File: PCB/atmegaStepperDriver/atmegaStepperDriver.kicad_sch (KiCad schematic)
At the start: 74 parts, among them J1 General power, J2 Motor Output, J3 Motor power, J4 Conn_01x05_Socket, J5 Reset Header, J6 I2C Communication pins, J9 Stepper communication pins, Q1 TIP42C, Q10 BC547, Q11 BC557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

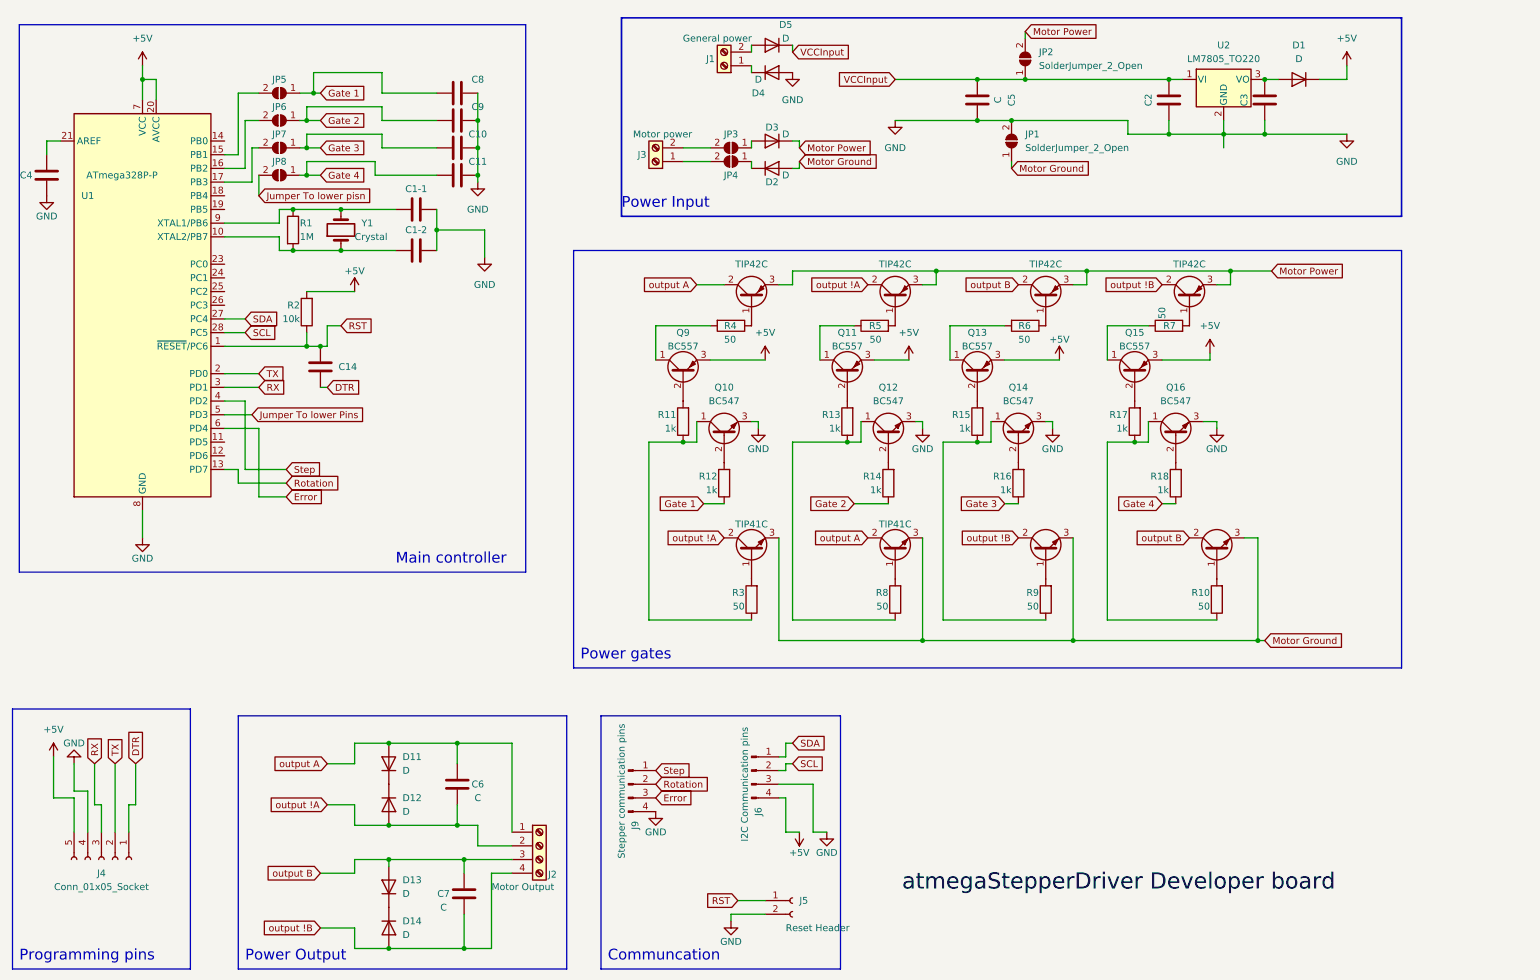
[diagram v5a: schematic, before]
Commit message: change capacitor footprint; added few pictures;
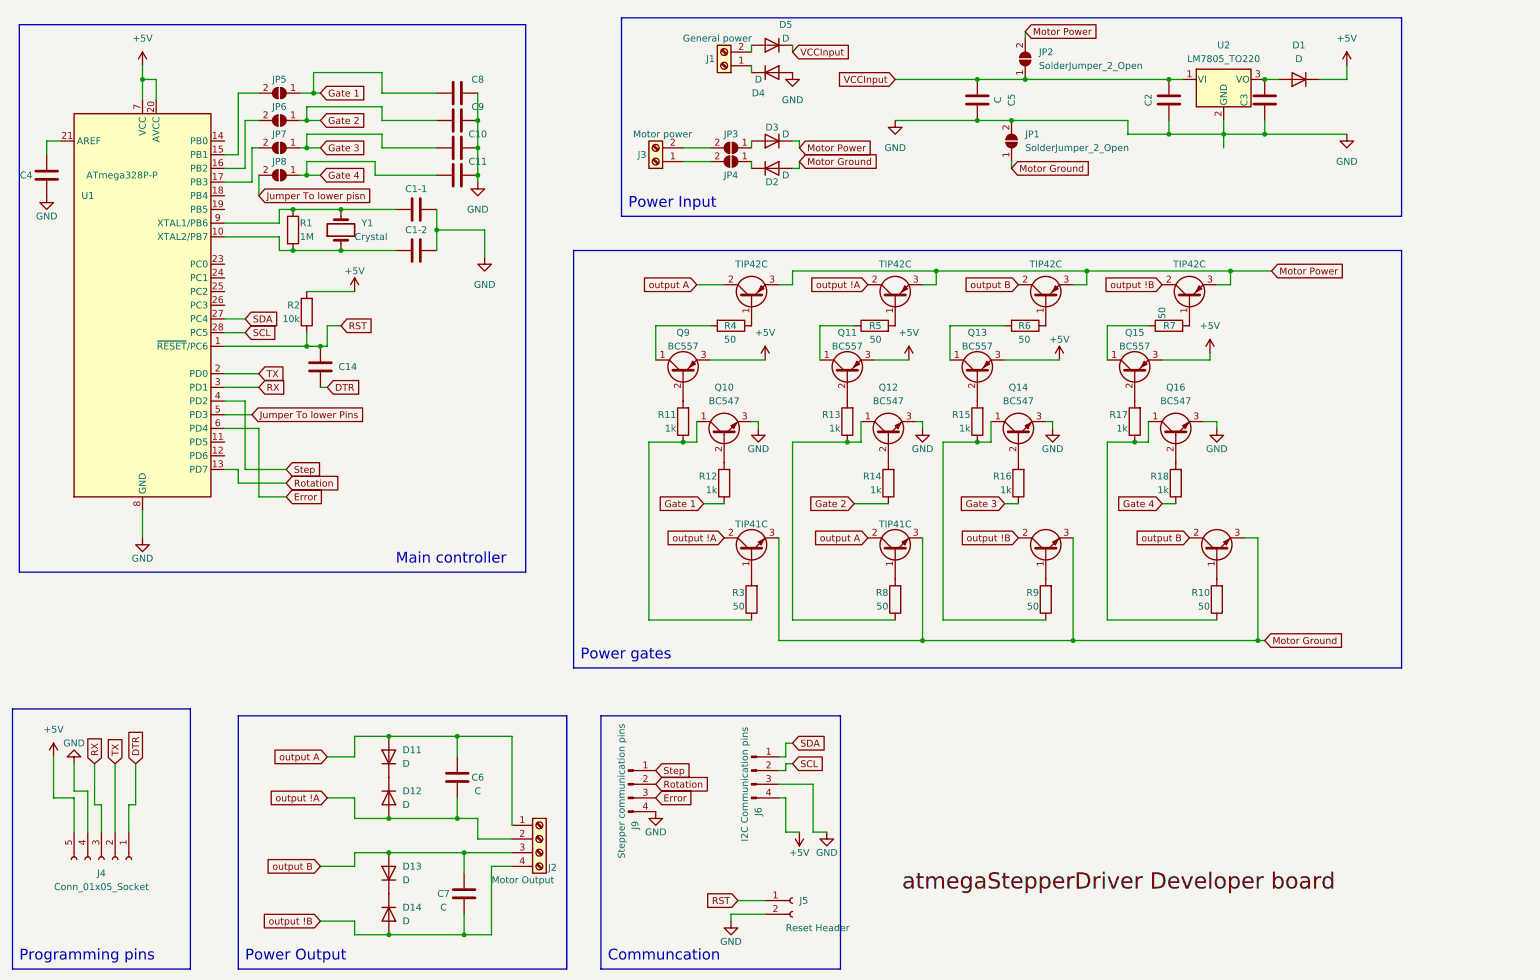
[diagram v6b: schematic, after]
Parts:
- C5: footprint Capacitor_THT:CP_Radial_Tantal_D9.0mm_P5.00mm -> Capacitor_THT:CP_Radial_D10.0mm_P5.00mm
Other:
- moved on the sheet: C6, D11, D12, D13, D14, J2

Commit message: All general connections ready; further check needed; V0.0.6
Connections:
- net Jumper To lower pisn is gone; now on net Jumper To lower Pins: JP8.2 (B)
- net GND: now also D2.2 (A), Q2.3 (E), Q6.3 (E), Q7.3 (E), Q8.3 (E)
- net Motor Ground: no longer D2.2 (A), Q2.3 (E), Q6.3 (E), Q7.3 (E), Q8.3 (E)
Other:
- moved on the sheet: C1-1, C1-2, C10, C11, C14, C2, C3, C4, C5, C6, C7, C8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

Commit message: Footprint done; ready for testing; drc clear; Gerber files;V0.7.1;
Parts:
- removed JP1: SolderJumper_2_Open, Jumper:SolderJumper-2_P1.3mm_Open_RoundedPad1.0x1.5mm, symbol Jumper:SolderJumper_2_Open
- added D6: D, Diode_THT:D_A-405_P7.62mm_Horizontal, symbol Device:D
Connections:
- net Motor Power: now also JP2.1 (A); no longer JP2.2 (B)
- net VCCInput: now also D6.2 (A); no longer JP2.1 (A)
- new net: D6.1 (K), JP2.2 (B)
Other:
- title: (none) -> atmegaStepperDriver Developer board
- moved on the sheet: JP2
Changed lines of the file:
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@@
   (paper "A4")
   (title_block
-    (date "2023-08-07")
-    (rev "0.0.6")
+    (title "atmegaStepperDriver Developer board")
+    (date "2023-08-09")
+    (rev "v0.7.1")
   )
   (junction (at 69.85 53.34) (diameter 0) (color 0 0 0 0)
@@
   (junction (at 76.2 59.69) (diameter 0) (color 0 0 0 0)
   )
-  (junction (at 195.58 29.21) (diameter 0) (color 0 0 0 0)
-  )
   (junction (at 71.12 38.1) (diameter 0) (color 0 0 0 0)
   )
@@
   (junction (at 81.28 165.1) (diameter 0) (color 0 0 0 0)
   )
+  (junction (at 194.31 29.21) (diameter 0) (color 0 0 0 0)
+  )
   (junction (at 195.58 92.71) (diameter 0) (color 0 0 0 0)
   )
@@
   (junction (at 81.28 143.51) (diameter 0) (color 0 0 0 0)
   )
-  (junction (at 193.04 36.83) (diameter 0) (color 0 0 0 0)
-  )
   (junction (at 81.28 180.34) (diameter 0) (color 0 0 0 0)
   )
@@
     (stroke (width 0) (type default))
   )
-  (wire (pts (xy 195.58 20.32) (xy 195.58 21.59))
+  (wire (pts (xy 195.58 20.32) (xy 194.31 20.32))
     (stroke (width 0) (type default))
   )
@@
     (stroke (width 0) (type default))
   )
+  (wire (pts (xy 179.07 20.32) (xy 179.07 26.67))
+    (stroke (width 0) (type default))
+  )
   (wire (pts (xy 57.15 110.49) (xy 66.04 110.49))
     (stroke (width 0) (type default))
@@
     (stroke (width 0) (type default))
   )
-  (wire (pts (xy 186.69 36.83) (xy 193.04 36.83))
+  (wire (pts (xy 186.69 36.83) (xy 214.63 36.83))
     (stroke (width 0) (type default))
   )
@@
     (stroke (width 0) (type default))
   )
-  (wire (pts (xy 195.58 29.21) (xy 222.25 29.21))
-    (stroke (width 0) (type default))
-  )
   (wire (pts (xy 58.42 43.18) (xy 58.42 52.07))
     (stroke (width 0) (type default))
@@
     (stroke (width 0) (type default))
   )
+  (wire (pts (xy 194.31 29.21) (xy 222.25 29.21))
+    (stroke (width 0) (type default))
+  )
   (wire (pts (xy 160.02 152.4) (xy 153.67 152.4))
     (stroke (width 0) (type default))
@@
     (stroke (width 0) (type default))
   )
-  (wire (pts (xy 193.04 36.83) (xy 214.63 36.83))
-    (stroke (width 0) (type default))
-  )
   (wire (pts (xy 198.12 88.9) (xy 198.12 92.71))
     (stroke (width 0) (type default))
@@
     (stroke (width 0) (type default))
   )
+  (wire (pts (xy 179.07 26.67) (xy 194.31 26.67))
+    (stroke (width 0) (type default))
+  )
   (wire (pts (xy 69.85 82.55) (xy 69.85 85.09))
     (stroke (width 0) (type default))
@@
     (stroke (width 0) (type default))
   )
+  (wire (pts (xy 194.31 26.67) (xy 194.31 29.21))
+    (stroke (width 0) (type default))
+  )
   (wire (pts (xy 69.85 50.8) (xy 69.85 53.34))
     (stroke (width 0) (type default))
@@
     (stroke (width 0) (type default))
   )
-  (wire (pts (xy 186.69 29.21) (xy 195.58 29.21))
+  (wire (pts (xy 186.69 29.21) (xy 194.31 29.21))
     (stroke (width 0) (type default))
   )
@@
     )
   )
-  (global_label "Motor Ground" (shape input) (at 193.04 45.72 0) (fields_autoplaced)
-    (effects (font (size 1.27 1.27)) (justify left))
-    (property "Intersheetrefs" "${INTERSHEET_REFS}" (at 208.9063 45.72 0)
-      (effects (font (size 1.27 1.27)) (justify left) hide)
-    )
-  )
   (global_label "output !B" (shape input) (at 203.2 110.49 180) (fields_autoplaced)
     (effects (font (size 1.27 1.27)) (justify right))
@@
     )
   )
-  (symbol (lib_id "Jumper:SolderJumper_2_Open") (at 193.04 40.64 90) (unit 1)
-    (in_bom yes) (on_board yes) (dnp no) (fields_autoplaced)
-    (property "Reference" "JP1" (at 195.58 39.37 90)
-      (effects (font (size 1.27 1.27)) (justify right))
-    )
-    (property "Value" "SolderJumper_2_Open" (at 195.58 41.91 90)
-      (effects (font (size 1.27 1.27)) (justify right))
-    )
-    (property "Footprint" "Jumper:SolderJumper-2_P1.3mm_Open_RoundedPad1.0x1.5mm" (at 193.04 40.64 0)
-      (effects (font (size 1.27 1.27)) hide)
-    )
-    (property "Datasheet" "~" (at 193.04 40.64 0)
-      (effects (font (size 1.27 1.27)) hide)
-    )
-    (pin "1")
-    (pin "2")
-    (instances
-      (project "atmegaStepperDriver"
-        (path "/c84e7e69-c1fd-4499-93bc-6ad0c4ebade1"
-          (reference "JP1") (unit 1)
-        )
-      )
-    )
-  )
   (symbol (lib_id "Transistor_BJT:BC557") (at 195.58 80.01 90) (unit 1)
     (in_bom yes) (on_board yes) (dnp no)
@@
     )
   )
-  (symbol (lib_id "Jumper:SolderJumper_2_Open") (at 195.58 25.4 90) (unit 1)
-    (in_bom yes) (on_board yes) (dnp no) (fields_autoplaced)
-    (property "Reference" "JP2" (at 198.12 24.13 90)
-      (effects (font (size 1.27 1.27)) (justify right))
-    )
-    (property "Value" "SolderJumper_2_Open" (at 198.12 26.67 90)
-      (effects (font (size 1.27 1.27)) (justify right))
-    )
-    (property "Footprint" "Jumper:SolderJumper-2_P1.3mm_Open_RoundedPad1.0x1.5mm" (at 195.58 25.4 0)
-      (effects (font (size 1.27 1.27)) hide)
-    )
-    (property "Datasheet" "~" (at 195.58 25.4 0)
+  (symbol (lib_id "Jumper:SolderJumper_2_Open") (at 190.5 20.32 180) (unit 1)
+    (in_bom yes) (on_board yes) (dnp no)
+    (property "Reference" "JP2" (at 193.04 25.4 0)
+      (effects (font (size 1.27 1.27)))
+    )
+    (property "Value" "SolderJumper_2_Open" (at 195.58 22.86 0)
+      (effects (font (size 1.27 1.27)))
+    )
+    (property "Footprint" "Jumper:SolderJumper-2_P1.3mm_Open_RoundedPad1.0x1.5mm" (at 190.5 20.32 0)
+      (effects (font (size 1.27 1.27)) hide)
+    )
+    (property "Datasheet" "~" (at 190.5 20.32 0)
       (effects (font (size 1.27 1.27)) hide)
     )
@@
         )
       )
+    )
+  )
+  (symbol (lib_id "Device:D") (at 182.88 20.32 180) (unit 1)
+    (in_bom yes) (on_board yes) (dnp no)
+    (property "Reference" "D6" (at 182.88 22.86 0)
+      (effects (font (size 1.27 1.27)))
+    )
+    (property "Value" "D" (at 185.42 19.05 0)
+      (effects (font (size 1.27 1.27)))
+    )
+    (property "Footprint" "Diode_THT:D_A-405_P7.62mm_Horizontal" (at 182.88 20.32 0)
+      (effects (font (size 1.27 1.27)) hide)
+    )
+    (property "Datasheet" "~" (at 182.88 20.32 0)
+      (effects (font (size 1.27 1.27)) hide)
+    )
+    (property "Sim.Device" "D" (at 182.88 20.32 0)
+      (effects (font (size 1.27 1.27)) hide)
+    )
+    (property "Sim.Pins" "1=K 2=A" (at 182.88 20.32 0)
+      (effects (font (size 1.27 1.27)) hide)
+    )
+    (pin "1")
+    (pin "2")
+    (instances
+      (project "atmegaStepperDriver"
+        (path "/c84e7e69-c1fd-4499-93bc-6ad0c4ebade1"
+          (reference "D6") (unit 1)
+        )
+      )
